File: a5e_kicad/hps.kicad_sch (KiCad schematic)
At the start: 5 parts, among them IC301 74AVC1T45GM-Q100H, IC302 74AVC1T45GM-Q100H, U1 A5EB013B-B23B, U301 MTFC4GLDDQ-4MIT

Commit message: add vias to lppdr balls
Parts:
- renumbered C301 to C7, IC301 to IC3, IC302 to IC4, U1 to U7, U301 to U8
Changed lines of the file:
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@@
 		(dnp no)
 		(fields_autoplaced yes)
-		(property "Reference" "#PWR0302"
+		(property "Reference" "#PWR040"
 			(at 27.94 54.61 0)
 			(hide yes)
@@
 			(project "agilex_3_soc"
 				(path "/a5b98d95-6877-4284-904f-d04e32723ae0/1bba180f-a717-40d4-b2d6-e5a7b998021f"
-					(reference "#PWR0302")
+					(reference "#PWR040")
 					(unit 1)
 				)
@@
 		(dnp no)
 		(fields_autoplaced yes)
-		(property "Reference" "IC301"
+		(property "Reference" "IC3"
 			(at 69.85 132.08 0)
 			(show_name no)
@@
 			(project "agilex_3_soc"
 				(path "/a5b98d95-6877-4284-904f-d04e32723ae0/1bba180f-a717-40d4-b2d6-e5a7b998021f"
-					(reference "IC301")
+					(reference "IC3")
 					(unit 1)
 				)
@@
 		(in_pos_files yes)
 		(dnp no)
-		(property "Reference" "C301"
+		(property "Reference" "C7"
 			(at 50.8 97.79 0)
 			(show_name no)
@@
 			(project "agilex_3_soc"
 				(path "/a5b98d95-6877-4284-904f-d04e32723ae0/1bba180f-a717-40d4-b2d6-e5a7b998021f"
-					(reference "C301")
+					(reference "C7")
 					(unit 1)
 				)
@@
 		(dnp no)
 		(fields_autoplaced yes)
-		(property "Reference" "#PWR0308"
+		(property "Reference" "#PWR044"
 			(at 48.26 173.99 0)
 			(hide yes)
@@
 			(project "agilex_3_soc"
 				(path "/a5b98d95-6877-4284-904f-d04e32723ae0/1bba180f-a717-40d4-b2d6-e5a7b998021f"
-					(reference "#PWR0308")
+					(reference "#PWR044")
 					(unit 1)
 				)
@@
 		(dnp no)
 		(fields_autoplaced yes)
-		(property "Reference" "#PWR0301"
+		(property "Reference" "#PWR042"
 			(at 33.02 54.61 0)
 			(hide yes)
@@
 			(project "agilex_3_soc"
 				(path "/a5b98d95-6877-4284-904f-d04e32723ae0/1bba180f-a717-40d4-b2d6-e5a7b998021f"
-					(reference "#PWR0301")
+					(reference "#PWR042")
 					(unit 1)
 				)
@@
 		(dnp no)
 		(fields_autoplaced yes)
-		(property "Reference" "#PWR0306"
+		(property "Reference" "#PWR047"
 			(at 88.9 140.97 0)
 			(hide yes)
@@
 			(project "agilex_3_soc"
 				(path "/a5b98d95-6877-4284-904f-d04e32723ae0/1bba180f-a717-40d4-b2d6-e5a7b998021f"
-					(reference "#PWR0306")
+					(reference "#PWR047")
 					(unit 1)
 				)
@@
 		(dnp no)
 		(fields_autoplaced yes)
-		(property "Reference" "#PWR0304"
+		(property "Reference" "#PWR043"
 			(at 33.02 110.49 0)
 			(hide yes)
@@
 			(project "agilex_3_soc"
 				(path "/a5b98d95-6877-4284-904f-d04e32723ae0/1bba180f-a717-40d4-b2d6-e5a7b998021f"
-					(reference "#PWR0304")
+					(reference "#PWR043")
 					(unit 1)
 				)
@@
 		(in_pos_files yes)
 		(dnp no)
-		(property "Reference" "IC302"
+		(property "Reference" "IC4"
 			(at 69.85 149.86 0)
 			(show_name no)
@@
 			(project "agilex_3_soc"
 				(path "/a5b98d95-6877-4284-904f-d04e32723ae0/1bba180f-a717-40d4-b2d6-e5a7b998021f"
-					(reference "IC302")
+					(reference "IC4")
 					(unit 1)
 				)
@@
 		(dnp no)
 		(fields_autoplaced yes)
-		(property "Reference" "#PWR0309"
+		(property "Reference" "#PWR048"
 			(at 91.44 173.99 0)
 			(hide yes)
@@
 			(project "agilex_3_soc"
 				(path "/a5b98d95-6877-4284-904f-d04e32723ae0/1bba180f-a717-40d4-b2d6-e5a7b998021f"
-					(reference "#PWR0309")
+					(reference "#PWR048")
 					(unit 1)
 				)
@@
 		(dnp no)
 		(fields_autoplaced yes)
-		(property "Reference" "#PWR0303"
+		(property "Reference" "#PWR041"
 			(at 27.94 110.49 0)
 			(hide yes)
@@
 			(project "agilex_3_soc"
 				(path "/a5b98d95-6877-4284-904f-d04e32723ae0/1bba180f-a717-40d4-b2d6-e5a7b998021f"
-					(reference "#PWR0303")
+					(reference "#PWR041")
 					(unit 1)
 				)
@@
 		(dnp no)
 		(fields_autoplaced yes)
-		(property "Reference" "#PWR0307"
+		(property "Reference" "#PWR046"
 			(at 50.8 140.97 0)
 			(hide yes)
@@
 			(project "agilex_3_soc"
 				(path "/a5b98d95-6877-4284-904f-d04e32723ae0/1bba180f-a717-40d4-b2d6-e5a7b998021f"
-					(reference "#PWR0307")
+					(reference "#PWR046")
 					(unit 1)
 				)
@@
 		(dnp no)
 		(fields_autoplaced yes)
-		(property "Reference" "#PWR0305"
+		(property "Reference" "#PWR045"
 			(at 50.8 110.49 0)
 			(hide yes)
@@
 			(project "agilex_3_soc"
 				(path "/a5b98d95-6877-4284-904f-d04e32723ae0/1bba180f-a717-40d4-b2d6-e5a7b998021f"
-					(reference "#PWR0305")
+					(reference "#PWR045")
 					(unit 1)
 				)
@@
 		(in_pos_files yes)
 		(dnp no)
-		(property "Reference" "U301"
+		(property "Reference" "U8"
 			(at 40.64 53.34 0)
 			(show_name no)
@@
 			(project "agilex_3_soc"
 				(path "/a5b98d95-6877-4284-904f-d04e32723ae0/1bba180f-a717-40d4-b2d6-e5a7b998021f"
-					(reference "U301")
+					(reference "U8")
 					(unit 1)
 				)
@@
 		(dnp no)
 		(fields_autoplaced yes)
-		(property "Reference" "U1"
+		(property "Reference" "U7"
 			(at 256.54 90.3576 0)
 			(show_name no)
@@
 			(project "agilex_3_soc"
 				(path "/a5b98d95-6877-4284-904f-d04e32723ae0/1bba180f-a717-40d4-b2d6-e5a7b998021f"
-					(reference "U1")
+					(reference "U7")
 					(unit 2)
 				)

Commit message: add comments
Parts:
- removed U8: MTFC4GLDDQ-4MIT, PCAD_import:MTFC4GLDDQ-4MIT_1, symbol PCAD_import:MTFC4GLDDQ-4MIT
- added J8: Micro_SD_Card, Connector_Card:microSD_HC_Wuerth_693072010801, symbol Connector:Micro_SD_Card
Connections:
- net sd_clk: now also J8.5 (CLK)
- net sd_cmd: now also J8.3 (CMD)
- net sd_d0: now also J8.7 (DAT0)
- net sd_d1: now also J8.8 (DAT1)
- net sd_d2: now also J8.1 (DAT2)
- net sd_d3: now also J8.2 (DAT3/CD)

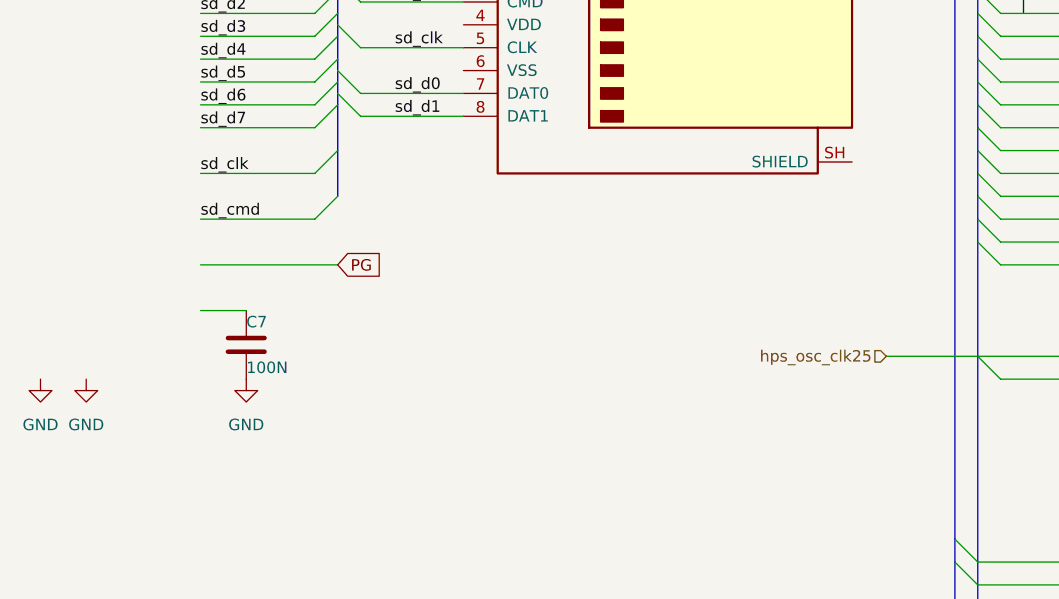
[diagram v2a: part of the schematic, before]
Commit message: remove extra components and make 1v8 plane
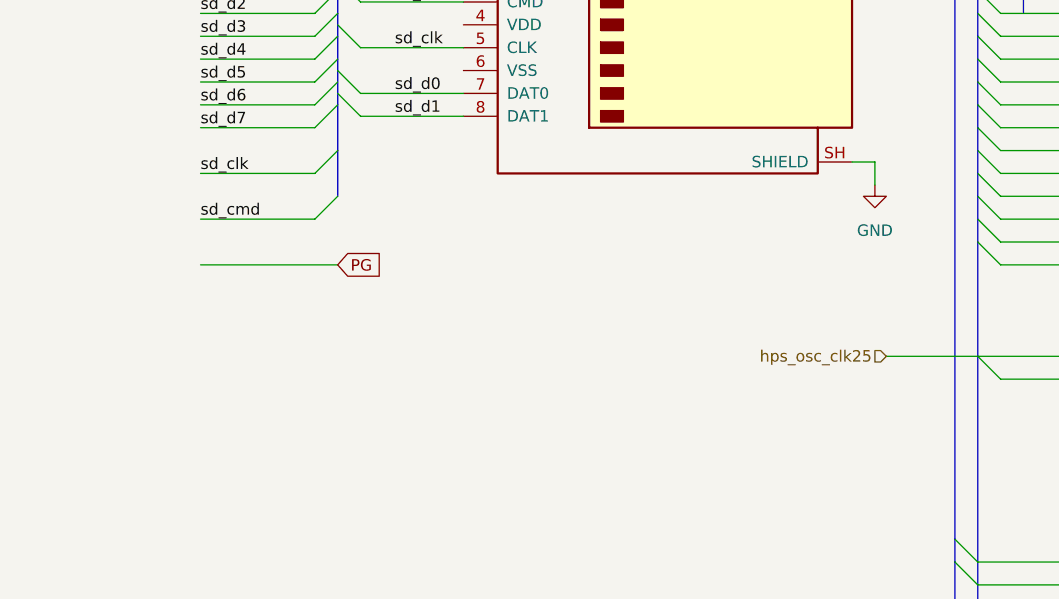
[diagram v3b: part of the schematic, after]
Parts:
- removed C7: 100N, Capacitor_SMD:C_0402_1005Metric, symbol Device:C
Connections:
- net GND: now also J8.SH (SHIELD)

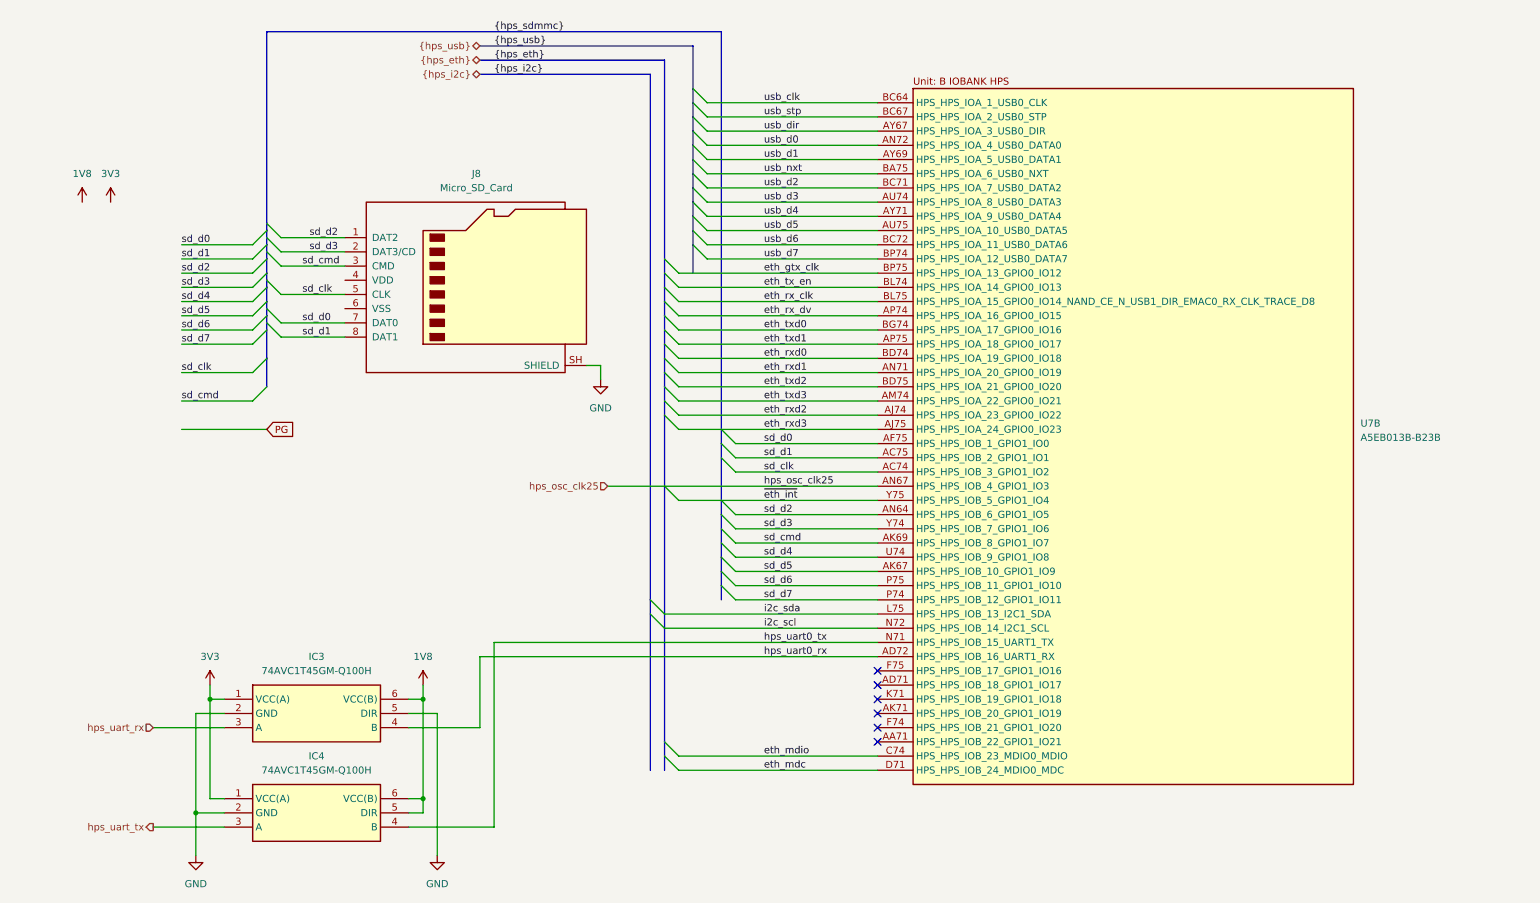
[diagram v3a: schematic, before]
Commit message: add sdcard level shifter
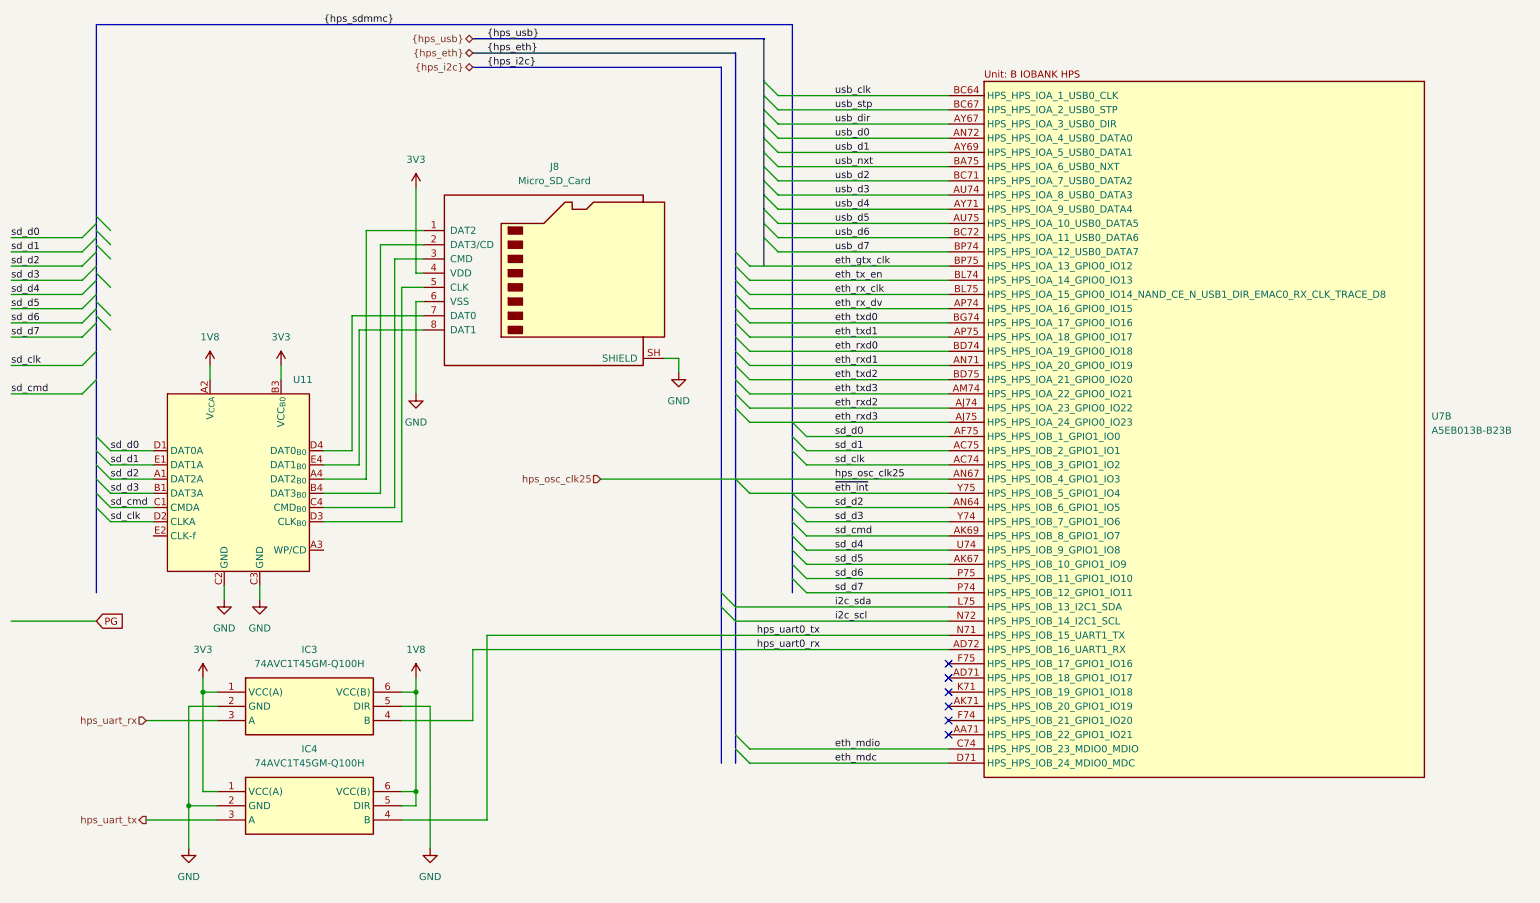
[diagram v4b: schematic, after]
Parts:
- added U11: (no value), Package_BGA:Texas_YFP0020_DSBGA-20_1.588x1.988mm_Layout4x5_P0.4mm, symbol agilex_5_lib:TXS0206A
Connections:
- net 1V8: now also U11.A2 (V_{CCA})
- net 3V3: now also J8.4 (VDD), U11.B3 (VCC_{B0})
- net GND: now also J8.6 (VSS), U11.C2 (GND), U11.C3 (GND)
- net sd_clk: now also U11.D2 (CLKA); no longer J8.5 (CLK)
- net sd_cmd: now also U11.C1 (CMDA); no longer J8.3 (CMD)
- net sd_d0: now also U11.D1 (DAT0A); no longer J8.7 (DAT0)
- net sd_d1: now also U11.E1 (DAT1A); no longer J8.8 (DAT1)
- net sd_d2: now also U11.A1 (DAT2A); no longer J8.1 (DAT2)
- net sd_d3: now also U11.B1 (DAT3A); no longer J8.2 (DAT3/CD)
- new net: J8.1 (DAT2), U11.A4 (DAT2_{B0})
- new net: J8.2 (DAT3/CD), U11.B4 (DAT3_{B0})
- new net: J8.3 (CMD), U11.C4 (CMD_{B0})
- new net: J8.5 (CLK), U11.D3 (CLK_{B0})
- new net: J8.7 (DAT0), U11.D4 (DAT0_{B0})
- new net: J8.8 (DAT1), U11.E4 (DAT1_{B0})
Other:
- moved on the sheet: IC3, IC4, J8, U7B

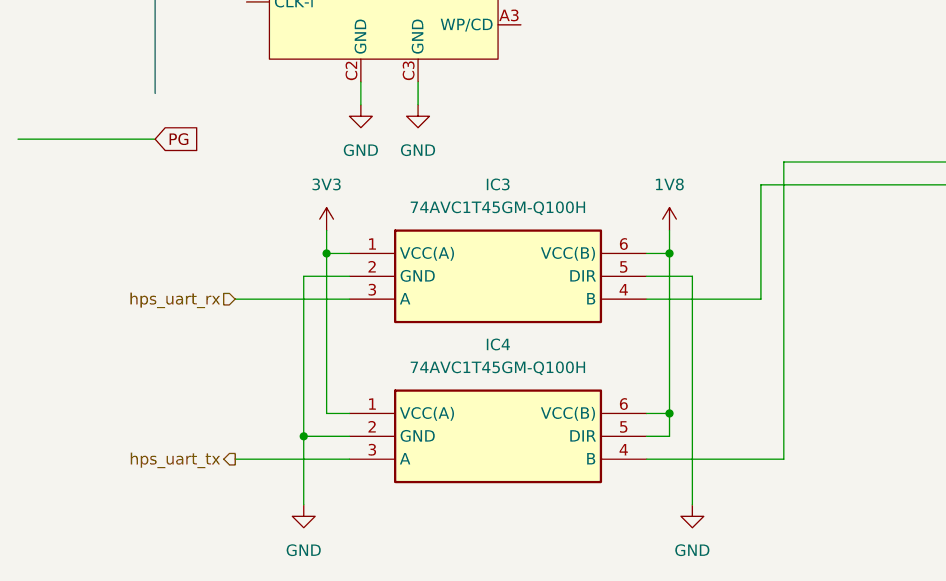
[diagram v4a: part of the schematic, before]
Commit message: add resistors for ad channels
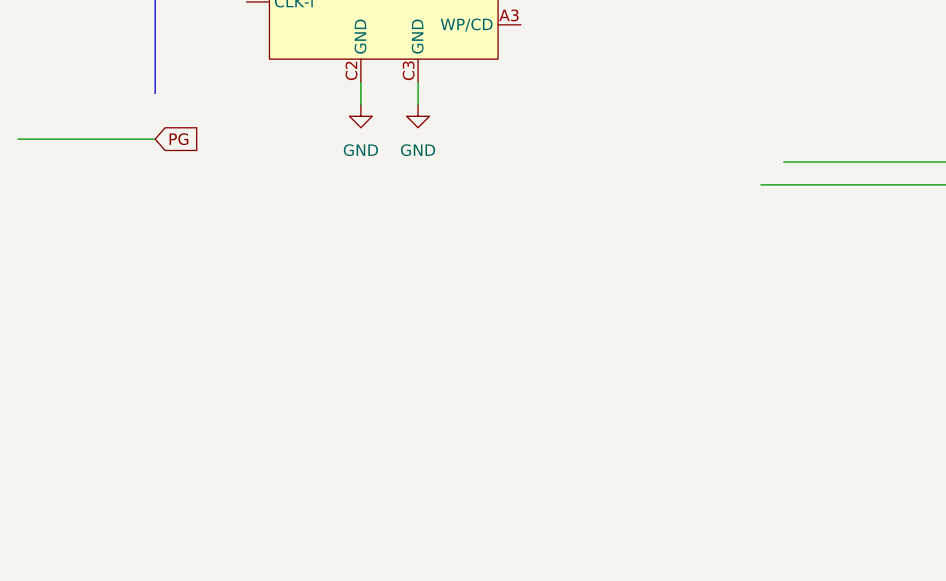
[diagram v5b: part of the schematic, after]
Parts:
- removed IC3, IC4: 74AVC1T45GM-Q100H, symbol 74AVC1T45GM-Q100H:74AVC1T45GM-Q100H
